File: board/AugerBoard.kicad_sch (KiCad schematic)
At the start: 0 parts

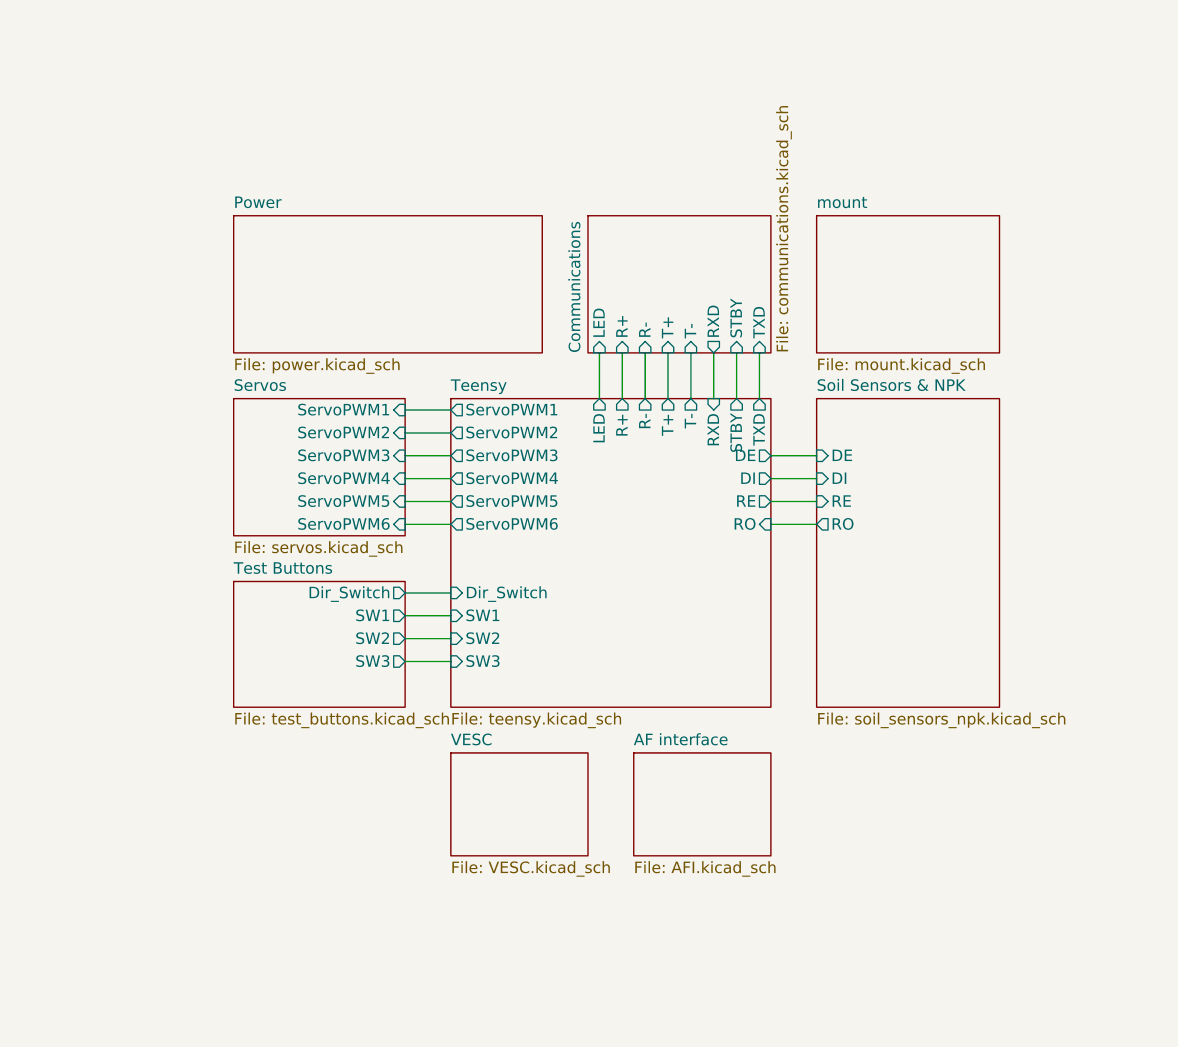
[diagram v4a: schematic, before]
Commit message: Soil sensors pt. 2
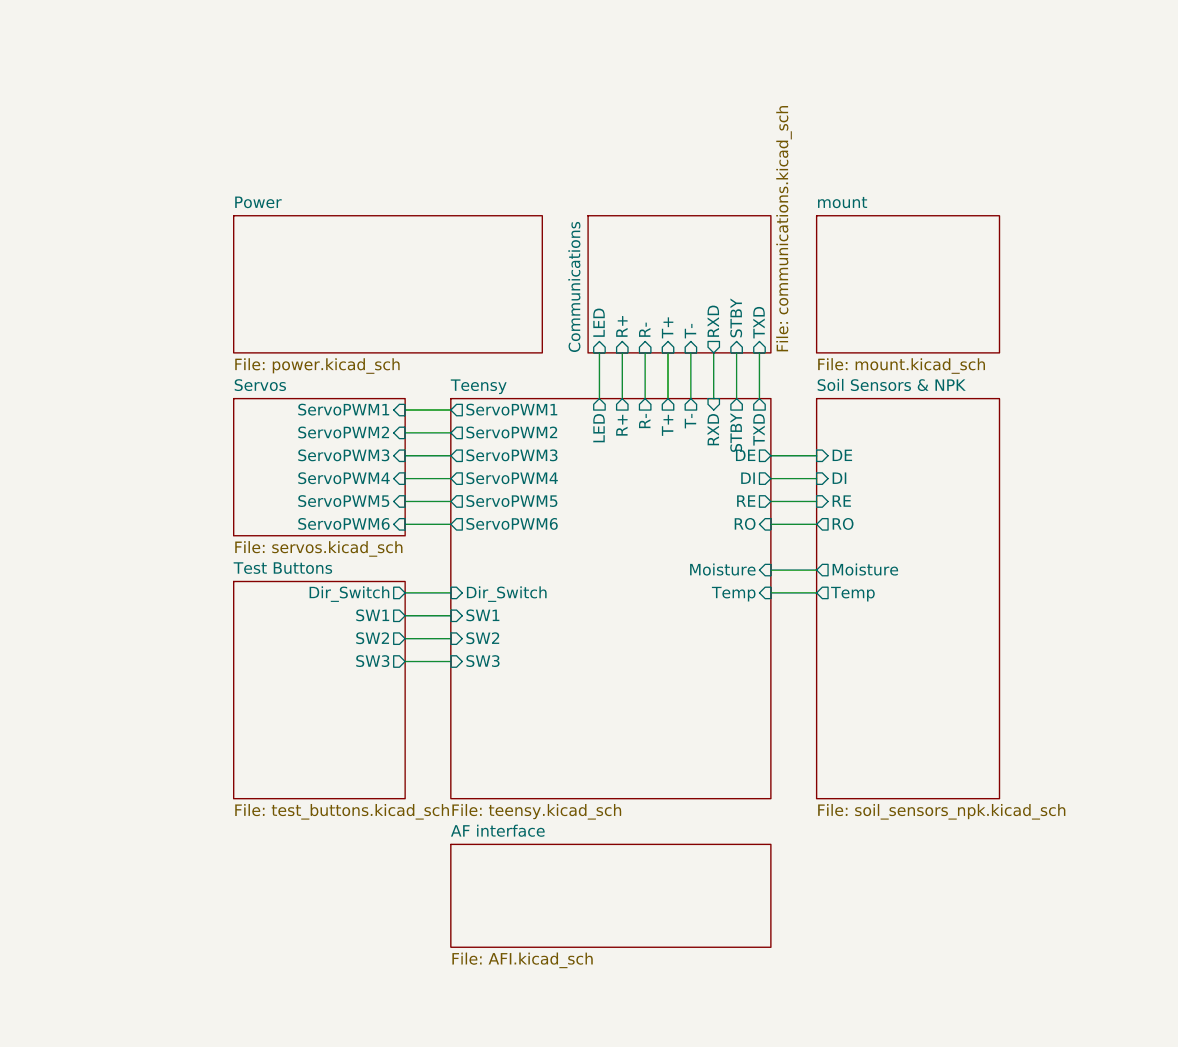
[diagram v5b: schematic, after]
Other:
- removed sheet VESC
- sheet Soil Sensors & NPK ports: added Moisture, Temp; removed none
- sheet Teensy ports: added Moisture, Temp; removed none
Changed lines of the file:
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@@
+	(wire
+		(pts
+			(xy 161.29 99.06) (xy 166.37 99.06)
+		)
+		(stroke
+			(width 0)
+			(type default)
+		)
+	)
 	(wire
 		(pts
@@
 		(pts
 			(xy 144.78 74.93) (xy 144.78 80.01)
+		)
+		(stroke
+			(width 0)
+			(type default)
+		)
+	)
+	(wire
+		(pts
+			(xy 161.29 101.6) (xy 166.37 101.6)
 		)
 		(stroke
@@
 	(sheet
 		(at 125.73 80.01)
-		(size 35.56 34.29)
+		(size 35.56 44.45)
 		(exclude_from_sim no)
 		(in_bom yes)
@@
 		)
 		(property "Sheetfile" "teensy.kicad_sch"
-			(at 125.73 114.8846 0)
+			(at 125.73 125.0446 0)
 			(effects
 				(font
@@
 		(pin "RO" input
 			(at 161.29 93.98 0)
+			(effects
+				(font
+					(size 1.27 1.27)
+				)
+				(justify right)
+			)
+		)
+		(pin "Moisture" input
+			(at 161.29 99.06 0)
+			(effects
+				(font
+					(size 1.27 1.27)
+				)
+				(justify right)
+			)
+		)
+		(pin "Temp" input
+			(at 161.29 101.6 0)
 			(effects
 				(font
@@
 	(sheet
 		(at 101.6 100.33)
-		(size 19.05 13.97)
+		(size 19.05 24.13)
 		(exclude_from_sim no)
 		(in_bom yes)
@@
 		)
 		(property "Sheetfile" "test_buttons.kicad_sch"
-			(at 101.6 114.8846 0)
+			(at 101.6 125.0446 0)
 			(effects
 				(font
@@
 	)
 	(sheet
-		(at 146.05 119.38)
-		(size 15.24 11.43)
+		(at 125.73 129.54)
+		(size 35.56 11.43)
 		(exclude_from_sim no)
 		(in_bom yes)
@@
 		)
 		(property "Sheetname" "AF interface"
-			(at 146.05 118.6684 0)
+			(at 125.73 128.8284 0)
 			(effects
 				(font
@@
 		)
 		(property "Sheetfile" "AFI.kicad_sch"
-			(at 146.05 131.3946 0)
+			(at 125.73 141.5546 0)
 			(effects
 				(font
@@
 	)
 	(sheet
-		(at 125.73 119.38)
-		(size 15.24 11.43)
+		(at 166.37 80.01)
+		(size 20.32 44.45)
 		(exclude_from_sim no)
 		(in_bom yes)
@@
 			(color 0 0 0 0.0000)
 		)
-		(property "Sheetname" "VESC"
-			(at 125.73 118.6684 0)
-			(effects
-				(font
-					(size 1.27 1.27)
-				)
-				(justify left bottom)
-			)
-		)
-		(property "Sheetfile" "VESC.kicad_sch"
-			(at 125.73 131.3946 0)
-			(effects
-				(font
-					(size 1.27 1.27)
-				)
-				(justify left top)
-			)
-		)
-		(instances
-			(project "AugerBoard"
-				(path "/05fd3c2e-b986-4426-9c38-2a77d5c929de"
-					(page "8")
-				)
-			)
-		)
-	)
-	(sheet
-		(at 166.37 80.01)
-		(size 20.32 34.29)
-		(exclude_from_sim no)
-		(in_bom yes)
-		(on_board yes)
-		(dnp no)
-		(fields_autoplaced yes)
-		(stroke
-			(width 0.1524)
-			(type solid)
-		)
-		(fill
-			(color 0 0 0 0.0000)
-		)
 		(property "Sheetname" "Soil Sensors & NPK"
 			(at 166.37 79.2984 0)
@@
 		)
 		(property "Sheetfile" "soil_sensors_npk.kicad_sch"
-			(at 166.37 114.8846 0)
+			(at 166.37 125.0446 0)
 			(effects
 				(font
@@
 			(effects
 				(font
+					(size 1.27 1.27)
+				)
+				(justify left)
+			)
+		)
+		(pin "Moisture" output
+			(at 166.37 99.06 180)
+			(effects
+				(font
+					(size 1.27 1.27)
+				)
+				(justify left)
+			)
+		)
+		(pin "Temp" output
+			(at 166.37 101.6 180)
+			(effects
+				(font

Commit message: Added Labels, Missing Requirements, and Refined Look
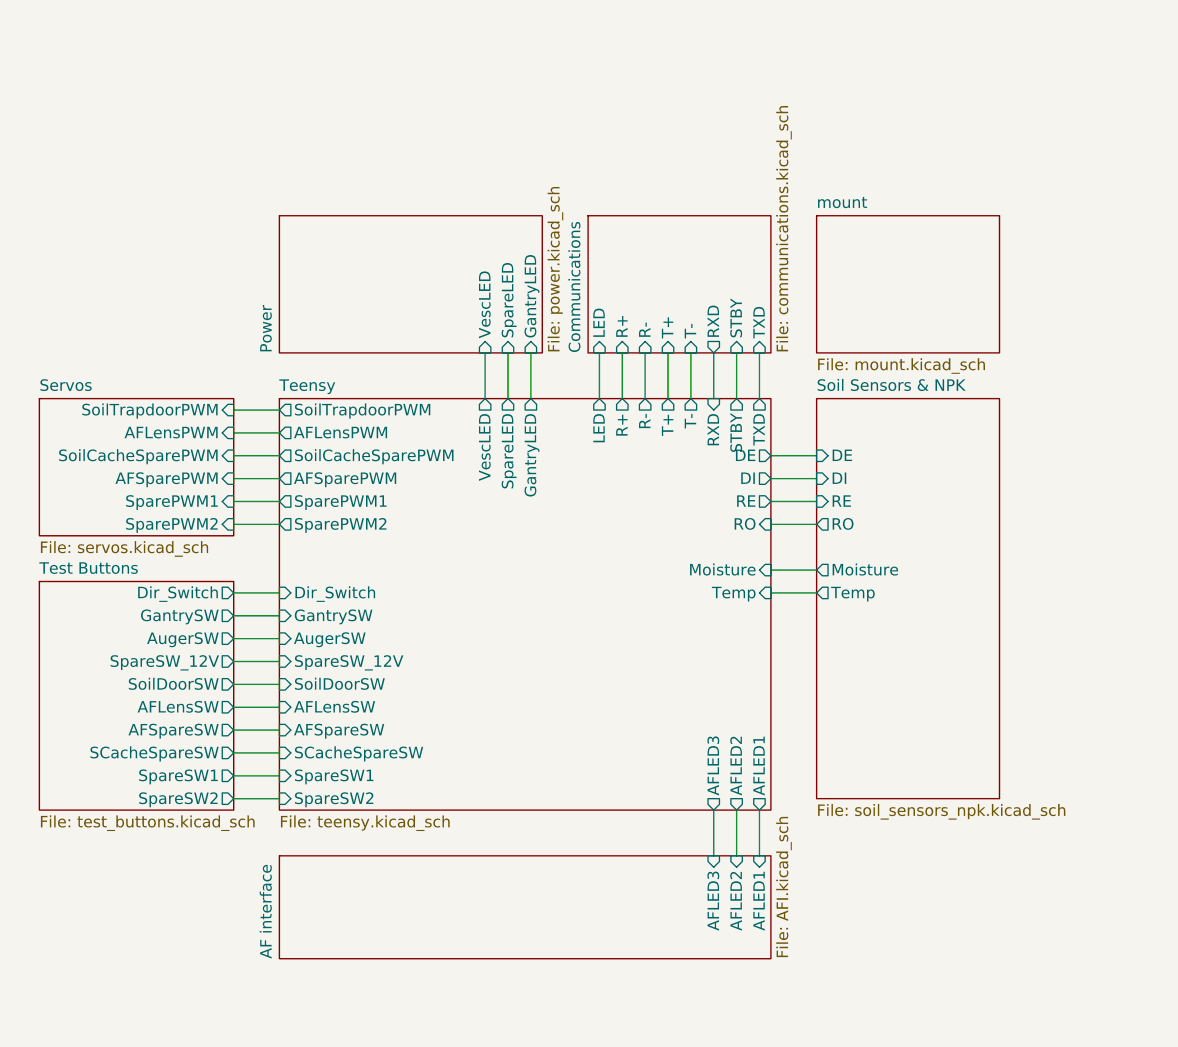
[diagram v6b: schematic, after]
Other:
- sheet AF interface ports: added AFLED1, AFLED2, AFLED3; removed none
- sheet Power ports: added GantryLED, SpareLED, VescLED; removed none
- sheet Servos ports: added AFLensPWM, AFSparePWM, SoilCacheSparePWM, SoilTrapdoorPWM, SparePWM1, SparePWM2; removed ServoPWM1, ServoPWM2, ServoPWM3, ServoPWM4, ServoPWM5, ServoPWM6
- sheet Teensy ports: added AFLED1, AFLED2, AFLED3, AFLensPWM, AFLensSW, AFSparePWM, AFSpareSW, AugerSW, GantryLED, GantrySW, SCacheSpareSW, SoilCacheSparePWM, SoilDoorSW, SoilTrapdoorPWM, SpareLED, SparePWM1, SparePWM2, SpareSW1, SpareSW2, SpareSW_12V, VescLED; removed SW1, SW2, SW3, ServoPWM1, ServoPWM2, ServoPWM3, ServoPWM4, ServoPWM5, ServoPWM6
- sheet Test Buttons ports: added AFLensSW, AFSpareSW, AugerSW, GantrySW, SCacheSpareSW, SoilDoorSW, SpareSW1, SpareSW2, SpareSW_12V; removed SW1, SW2, SW3

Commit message: Adjusted resistor values & renamed AF outputs
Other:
- sheet AF interface ports: added AFLED340, AFLED405, AFLED490; removed AFLED1, AFLED2, AFLED3
- sheet Teensy ports: added AFLED340, AFLED405, AFLED490; removed AFLED1, AFLED2, AFLED3
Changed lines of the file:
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@@
 			)
 		)
-		(pin "AFLED1" output
+		(pin "AFLED340" output
 			(at 160.02 125.73 270)
 			(effects
@@
 			)
 		)
-		(pin "AFLED2" output
+		(pin "AFLED405" output
 			(at 157.48 125.73 270)
 			(effects
@@
 			)
 		)
-		(pin "AFLED3" output
+		(pin "AFLED490" output
 			(at 154.94 125.73 270)
 			(effects
@@
 			)
 		)
-		(pin "AFLED1" input
+		(pin "AFLED340" input
 			(at 160.02 130.81 90)
 			(effects
@@
 			)
 		)
-		(pin "AFLED2" input
+		(pin "AFLED405" input
 			(at 157.48 130.81 90)
 			(effects
@@
 			)
 		)
-		(pin "AFLED3" input
+		(pin "AFLED490" input
 			(at 154.94 130.81 90)
 			(effects

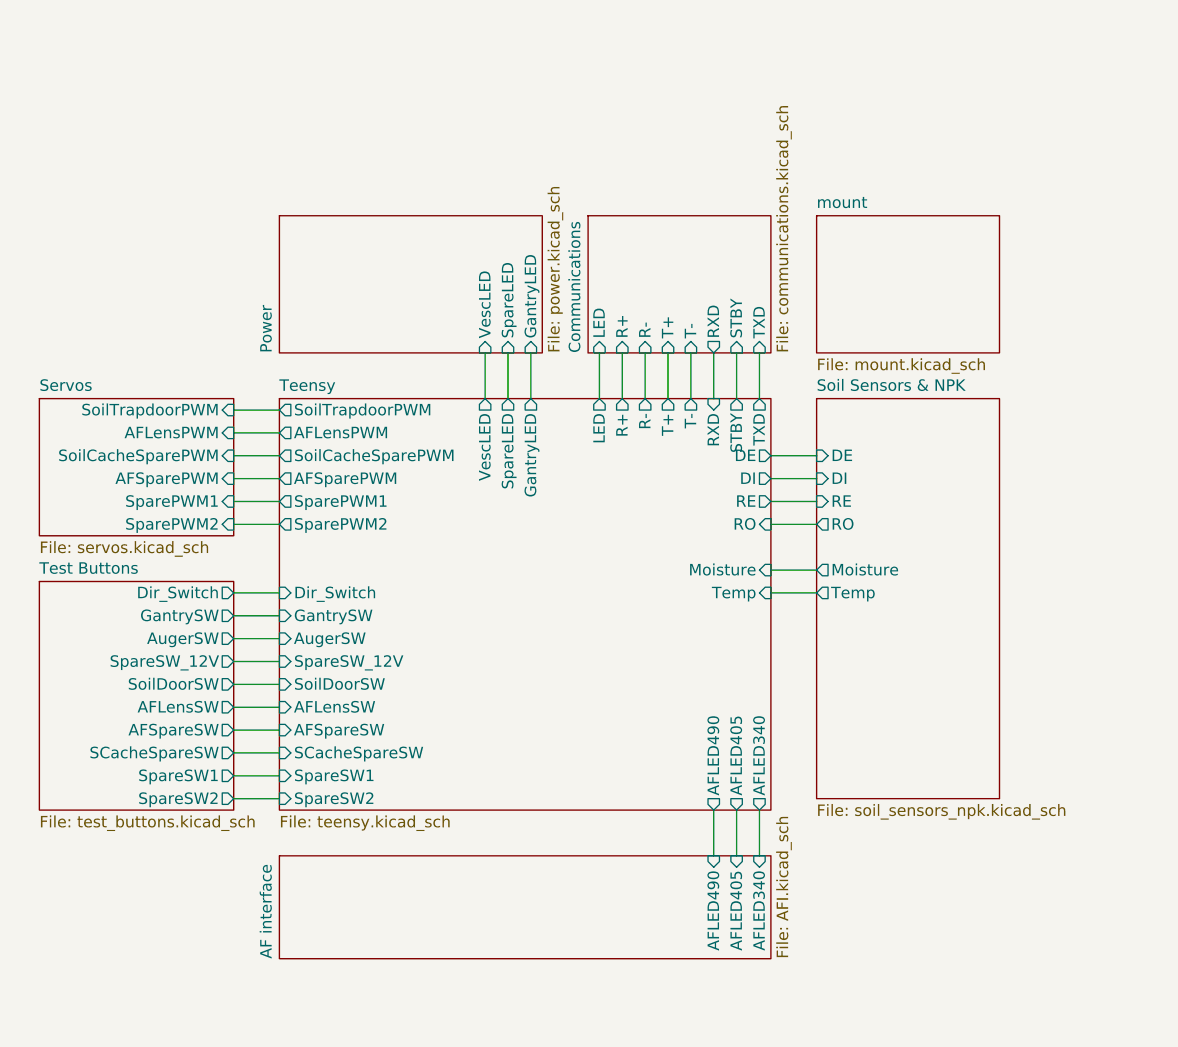
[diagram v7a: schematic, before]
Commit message: Fixed issues after schematic review
added 6 leds for every servo, changed txd and rxd to pins 30/31, added additional oki for 3.3V
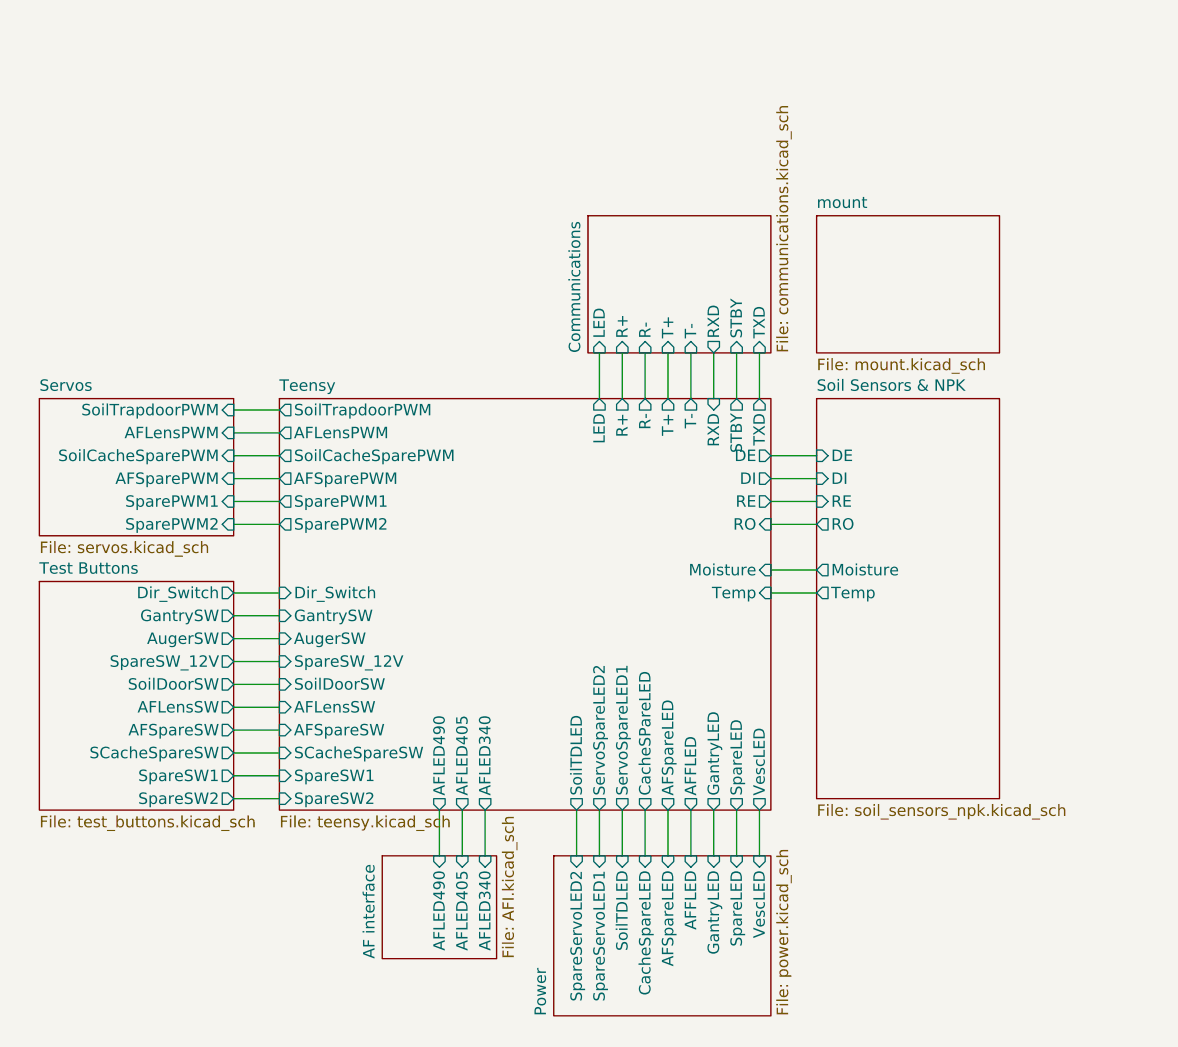
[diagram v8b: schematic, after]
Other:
- sheet Power ports: added AFFLED, AFSpareLED, CacheSpareLED, SoilTDLED, SpareServoLED1, SpareServoLED2; removed none
- sheet Teensy ports: added AFFLED, AFSpareLED, CacheSPareLED, ServoSpareLED1, ServoSpareLED2, SoilTDLED; removed none
